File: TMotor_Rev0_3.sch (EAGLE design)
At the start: 94 parts, among them J1 5015680507, J10 5015680207, J2 5015680507, J7 5015680207, J8 5015680207, J9 5015680207, Q1 IRLB8721PBFTO220H, Q2 IRLB8721PBFTO220H, Q3 IRLB8721PBFTO220H, Q4 IRLB8721PBFTO220H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

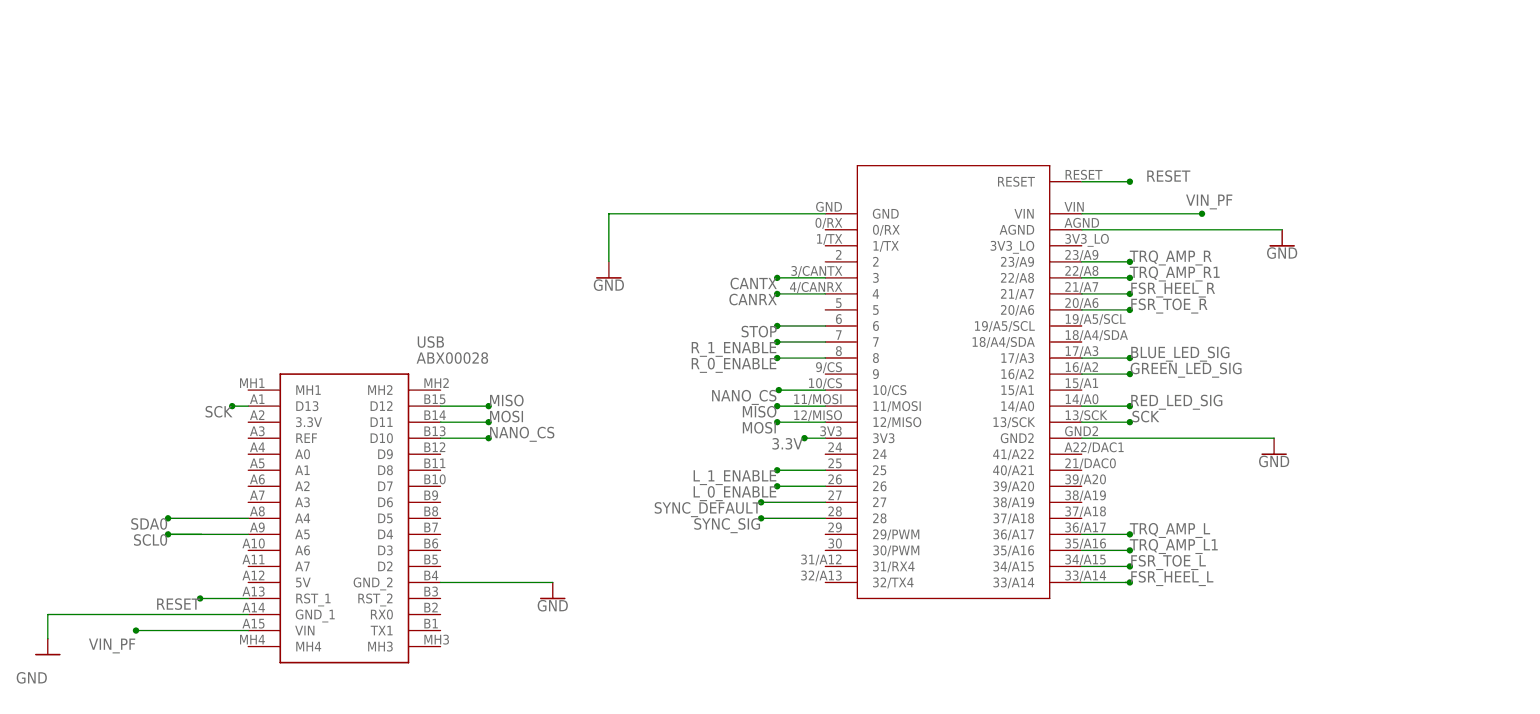
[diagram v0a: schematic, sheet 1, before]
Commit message: updated board to use Teensy 4.1
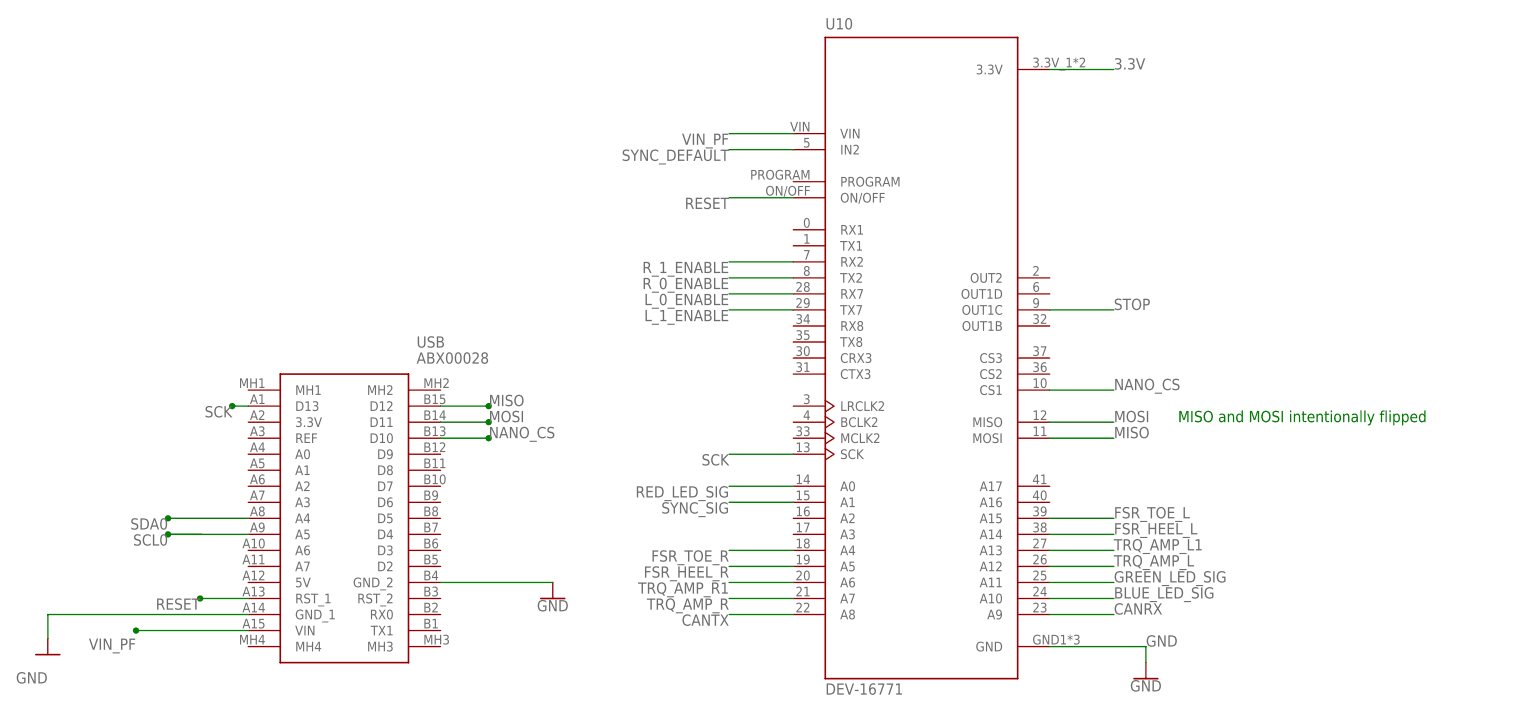
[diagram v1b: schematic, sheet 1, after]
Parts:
- removed U$1: TEENSY_3.5/3.6_EXTERNAL_W/RESET, Teensy356:TEENSY_3.5/3.6_EXTERNAL_W/RESET
- added J3: 5015680307, SnapEDA-Library:5015680307
- added U10: DEV-16771, SnapEDA-Library:DEV-16771
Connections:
- net 3.3V: now also U10.3.3V; no longer U$1.3V3
- net BLUE_LED_SIG: now also U10.A10; no longer U$1.17/A3
- net CANRX: now also U10.A9; no longer U$1.4
- net CANTX: now also U10.A8; no longer U$1.3
- net FSR_HEEL_L: now also U10.A14; no longer U$1.33/A14
- net FSR_HEEL_R: now also U10.A5; no longer U$1.21/A7
- net FSR_TOE_L: now also U10.A15; no longer U$1.34/A15
- net FSR_TOE_R: now also U10.A4; no longer U$1.20/A6
- net GND: now also U10.GND; no longer U$1.AGND, U$1.GND, U$1.GND2
- net GREEN_LED_SIG: now also U10.A11; no longer U$1.16/A2
- net L_0_ENABLE: now also U10.RX7; no longer U$1.26
- net L_1_ENABLE: now also U10.TX7; no longer U$1.25
- net MISO: now also U10.MOSI; no longer U$1.11/MOSI
- net MOSI: now also U10.MISO; no longer U$1.12/MISO
- net NANO_CS: now also U10.CS1; no longer U$1.10/CS
- net RED_LED_SIG: now also U10.A0; no longer U$1.14/A0
- net RESET: now also U10.ON/OFF; no longer U$1.RESET
- net R_0_ENABLE: now also U10.TX2; no longer U$1.8
- net R_1_ENABLE: now also U10.RX2; no longer U$1.7
- net SCK: now also U10.SCK; no longer U$1.13/SCK
- net SCL0: now also J3.3
- net SDA0: now also J3.1
- net STOP: now also U10.OUT1C; no longer U$1.6
- net SYNC_DEFAULT: now also U10.IN2; no longer U$1.27
- net SYNC_SIG: now also U10.A1; no longer U$1.28
- net TRQ_AMP_L: now also U10.A12; no longer U$1.36/A17
- net TRQ_AMP_L1: now also U10.A13; no longer U$1.35/A16
- net TRQ_AMP_R: now also U10.A7; no longer U$1.23/A9
- net TRQ_AMP_R1: now also U10.A6; no longer U$1.22/A8
- net VIN_PF: now also U10.VIN; no longer U$1.VIN
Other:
- note added: "MISO and MOSI intentionally flipped"
